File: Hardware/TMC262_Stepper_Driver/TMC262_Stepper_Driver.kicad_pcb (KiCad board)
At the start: 4 copper layers, 50 x 50 mm, 102 parts, among them J1 Conn_01x02, J3 629722000214, J4 Conn_01x04, J5 Conn_01x04, Q1 SQJ504EP, Q2 SQJ504EP, Q3 SQJ504EP, Q4 SQJ504EP, SW1 SW_Push, SW2 SW_Push, SW3 SW_Push, SW4 SW_Push, SW5 SW_Push, U2 AZ1117-3.3, U3 USBLC6-2SC6, U4 TMC262, U5 STM32G431CBUx

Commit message: stepper done
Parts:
- removed the C16 at (38.9, 124.2)
- removed the D12 at (52.5, 124.6)
- added C31: 1u, Capacitor_SMD:C_0402_1005Metric, F.Cu at (91.7, 69.1)
- added J6: Conn_01x05, Connector_JST:JST_PH_B5B-PH-K_1x05_P2.00mm_Vertical, F.Cu at (85.4, 65.2)
- added JP1: SolderJumper_3_Open, Jumper:SolderJumper-3_P2.0mm_Open_TrianglePad1.0x1.5mm, F.Cu at (87.7, 69.9)
- J5: renamed from J4; footprint Connector_JST:JST_EH_B4B-EH-A_1x04_P2.50mm_Vertical -> Connector_JST:JST_PH_B4B-PH-K_1x04_P2.00mm_Vertical
- Q1, Q2, Q3, Q4: footprint Maker:SQJ504EP -> Maker_librairy:SQJ504EP
- moved C16 63.9 mm to (91.9, 86.6), turned to -90 degrees
- moved C15 62.7 mm to (91.9, 81.3), turned to -90 degrees
- moved R8 55.6 mm to (80.1, 76.8)
- moved D2 52.3 mm to (96.0, 89.1)
- moved D1 51.8 mm to (96.0, 83.3)
- moved R19 45.6 mm to (59.6, 89.6), turned to 180 degrees
- moved R25 44.2 mm to (70.4, 74.7), turned to 90 degrees
- moved R20 43.7 mm to (59.6, 93.6), turned to 180 degrees
- moved R21 42.5 mm to (59.6, 97.6), turned to 180 degrees
- moved R28 42.4 mm to (90.4, 89.6)
- moved R26 39.9 mm to (69.4, 74.7), turned to 90 degrees
- moved Q2 38.6 mm to (64.7, 90.4), turned to -90 degrees
- moved R29 38.4 mm to (90.4, 93.6)
- moved D13 37.8 mm to (68.9, 77.2), turned to 90 degrees
- moved R30 34.9 mm to (90.4, 97.6)
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- renumbered C17 to C1, C29 to C10, C5 to C11, C6 to C12, C7 to C13, C3 to C14, C13 to C15, C15 to C16, C26 to C18, C30 to C19, C18 to C2, C11 to C20, C12 to C21, C14 to C22, C8 to C23, C9 to C24, C10 to C25, C27 to C26, C24 to C27, C23 to C29, C19 to C3, C4 to C30, C20 to C4, C21 to C5, C22 to C6, C1 to C7, C2 to C8, C25 to C9, D10 to D1, D9 to D10, D2 to D11, D3 to D12, D11 to D2, D1 to D4, D4 to D5, D5 to D6, D6 to D7, D7 to D8, D8 to D9, J5 to J1, J1 to J4, R26 to R1, R25 to R10, R30 to R11, R4 to R12, R7 to R13, R8 to R14, R9 to R15, R10 to R16, R11 to R17, R16 to R18, R29 to R2, R21 to R20, R23 to R21, R13 to R22, R5 to R23, R6 to R24, R14 to R25, R15 to R26, R17 to R27, R18 to R28, R20 to R29, R24 to R3, R22 to R30, R28 to R4, R2 to R5, R3 to R6, R1 to R7, R12 to R8, R27 to R9, SW3 to SW2, SW4 to SW3, SW2 to SW4, U2 to U1, U1 to U2, U5 to U3, U3 to U5
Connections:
- C29 pad 1: Net-(Q2A-S) -> Net-(Q3A-S)
- D2 pad 2: Net-(D11-DOUT) -> unconnected-(D2-DOUT-Pad2)
- J4 pad 1: +24V -> GND
- J4 pad 2: GND -> +24V
- Q2 pad 1: Net-(Q2A-S) -> Net-(Q1A-S)
- Q2 pad 2: /LB2 -> /LA1
- Q2 pad 4: /HB2 -> /HA1
- Q2 pad 5: /BMB2 -> /BMA1
- Q2 pad 6: /BMB2 -> /BMA1
- Q3 pad 1: Net-(Q1A-S) -> Net-(Q3A-S)
- Q3 pad 2: /LA1 -> /LB2
- Q3 pad 4: /HA1 -> /HB2
- Q3 pad 5: /BMA1 -> /BMB2
- Q3 pad 6: /BMA1 -> /BMB2
- Q4 pad 1: Net-(Q2A-S) -> Net-(Q3A-S)
- R27 pad 2: Net-(Q2A-S) -> Net-(Q3A-S)
- R28 pad 1: Net-(Q2A-S) -> Net-(Q3A-S)
- R29 pad 1: Net-(Q2A-S) -> Net-(Q3A-S)
- R30 pad 1: Net-(Q2A-S) -> Net-(Q3A-S)
- U2 pad 10: unconnected-(U1-AGND-Pad10) -> GND
- U2 pad 13: unconnected-(U1-PGND-Pad13) -> GND
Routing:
- net GND: track 0.00 -> 84.4 mm, vias 0 -> 147
- net +24V: track 0.00 -> 66.8 mm, vias 0 -> 30
- net +5V: track 0.00 -> 53.8 mm, vias 0 -> 10
- net /5V_USB: track 0.00 -> 45.0 mm, vias 0 -> 5
- net +3.3V: track 0.00 -> 37.4 mm, vias 0 -> 19
- net /VCP_RX: track 0.00 -> 35.3 mm, vias 0 -> 2
- net /BOOT_0: track 0.00 -> 27.7 mm, vias 0 -> 2
- net /ENC_Z: track 0.00 -> 27.0 mm, vias 0 -> 1
- net /5V_UART: track 0.00 -> 26.8 mm, vias 0 -> 1
- net /VCP_TX: track 0.00 -> 25.3 mm, vias 0 -> 2
- net /HA2: track 0.00 -> 21.1 mm, vias 0 -> 2
- net /SWDIO: track 0.00 -> 21.1 mm
- net /SWO: track 0.00 -> 20.5 mm
- net /SWCLK: track 0.00 -> 19.9 mm
- net Net-(D1-DIN): track 0.00 -> 19.9 mm
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- added copper zone on F.Cu, net +24V
- added copper zone on In2.Cu, net +24V
- added copper zone on In2.Cu, net +3.3V
- added copper zone on In2.Cu, net +5V
- added copper zone on F.Cu, net /5V_BUCK
- added copper zone on In2.Cu, net /5V_USB
- added copper zone on F.Cu, net /BMA1
- added copper zone on F.Cu, net /BMA2
- added copper zone on F.Cu, net /BMB1
- added copper zone on F.Cu, net /BMB2
- added copper zone on F.Cu, net Net-(Q1A-S)
- added copper zone on F.Cu, net Net-(Q3A-S)
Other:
- board text added: "3V3"
- board text added: "5V"
- board text added: "5VB"
- board text added: "5VE"
- board text added: "5VU"
- board text added: "A1"
- board text added: "A2"
- board text added: "B0"
- board text added: "B1"
- board text added: "B2"
- board text added: "BOOT"
- board text added: "GND A B Z VCC"
- board text added: "LED0 LED1"
- board text added: "NRST"
- board text added: "Vin"

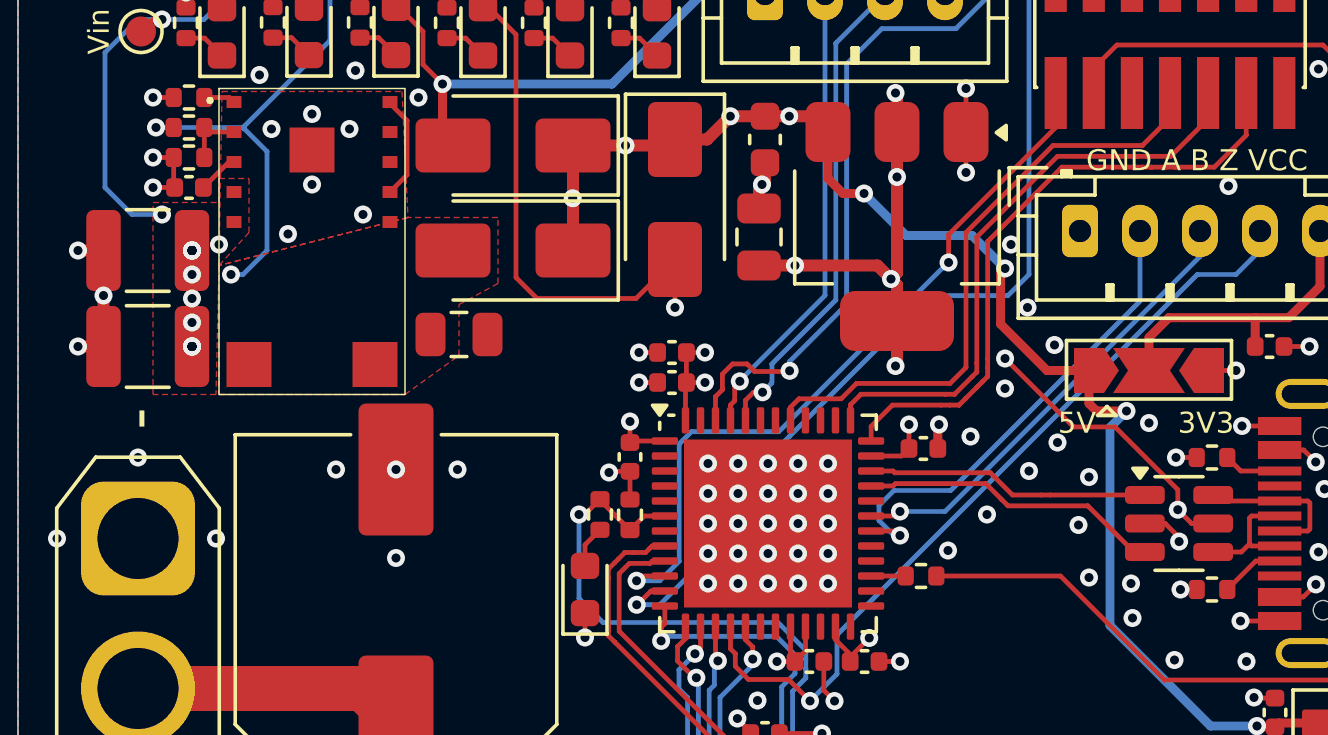
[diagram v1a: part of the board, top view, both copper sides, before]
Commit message: tune length usb, add teardrops
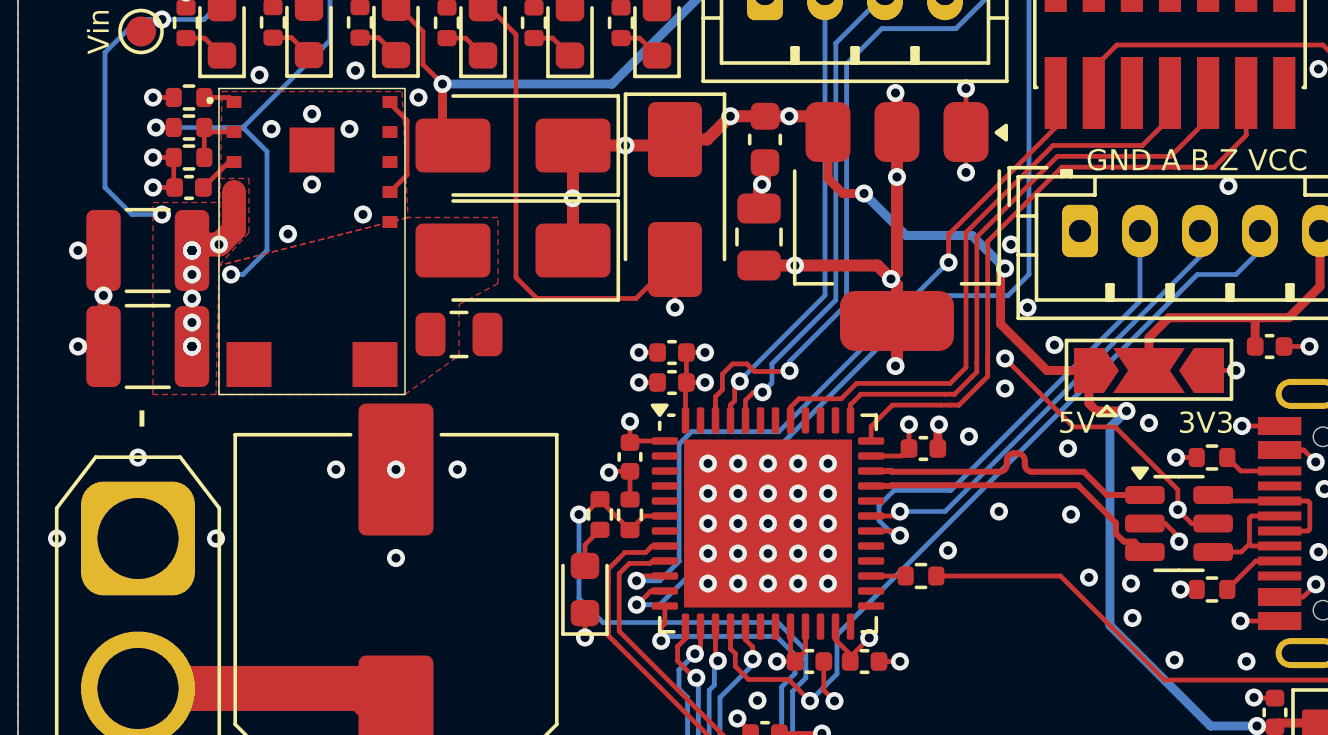
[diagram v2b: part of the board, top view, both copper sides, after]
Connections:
- net /USB_DM renamed /USB_DN
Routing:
- net +24V: track 66.8 -> 69.8 mm
- net /USB_DP: track 9.46 -> 10.2 mm
- net GND: vias 147 -> 144
- net (no net): vias 0 -> 1

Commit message: add pcb com
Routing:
- net +3.3V: track 37.4 -> 38.3 mm
- net GND: vias 144 -> 146
